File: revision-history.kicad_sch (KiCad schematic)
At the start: 0 parts

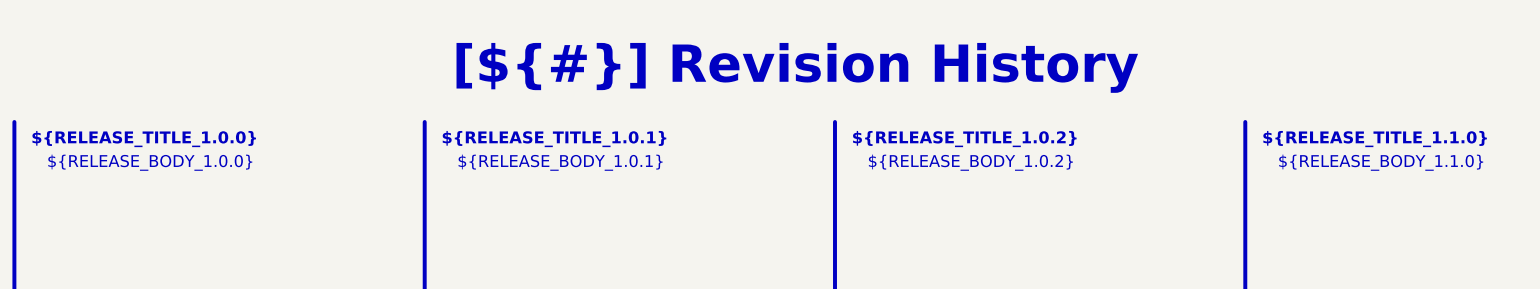
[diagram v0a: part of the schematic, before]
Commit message: feat: convert template to Boardwright
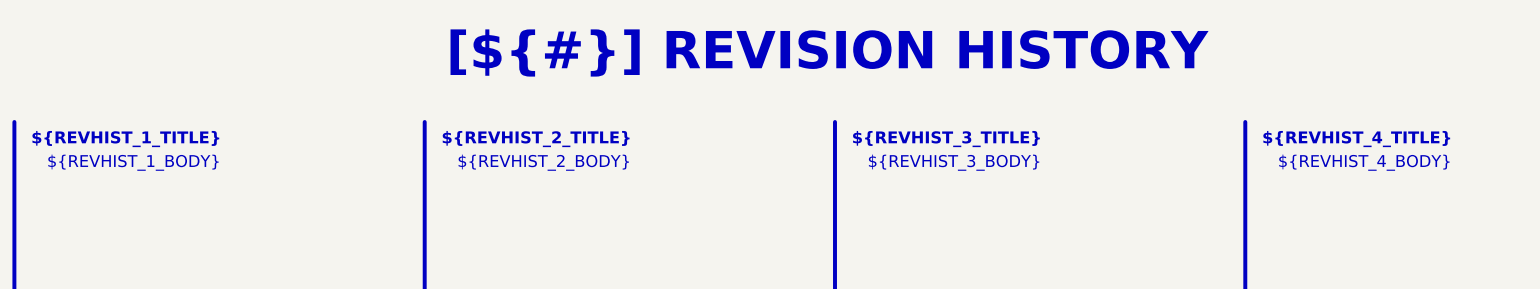
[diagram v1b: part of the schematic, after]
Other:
- title: Revision History -> REVISION HISTORY
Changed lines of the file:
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@@
 	(paper "A4")
 	(title_block
-		(title "Revision History")
+		(title "REVISION HISTORY")
 		(date "2025-01-12")
 		(rev "${REVISION}")
 		(company "${COMPANY}")
 	)
-	(text_box "${RELEASE_BODY_1.1.0}"
+	(text_box "${REVHIST_4_BODY}"
 		(exclude_from_sim no)
 		(at 224.79 35.56 0)
@@
 		(stroke
 			(width -0.0001)
-			(type default)
+			(type solid)
 		)
 		(fill
@@
 	(text_box "[${#}] ${TITLE}"
 		(exclude_from_sim no)
-		(at 80.01 15 0)
-		(size 137.16 15)
+		(at 20.32 10.16 0)
+		(size 266.7 20.32)
 		(margins 4.4999 4.4999 4.4999 4.4999)
 		(stroke
@@
 		)
 	)
-	(text_box "${RELEASE_BODY_1.0.0}"
+	(text_box "${REVHIST_1_BODY}"
 		(exclude_from_sim no)
 		(at 26.67 35.56 0)
@@
 		(stroke
 			(width -0.0001)
-			(type default)
+			(type solid)
 		)
 		(fill
@@
 		)
 	)
-	(text_box "${RELEASE_TITLE_1.0.2}"
+	(text_box "${REVHIST_3_TITLE}"
 		(exclude_from_sim no)
 		(at 156.21 31.75 0)
@@
 		(stroke
 			(width -0.0001)
-			(type default)
+			(type solid)
 		)
 		(fill
@@
 		)
 	)
-	(text_box "${RELEASE_BODY_1.0.2}"
+	(text_box "${REVHIST_3_BODY}"
 		(exclude_from_sim no)
 		(at 158.75 35.56 0)
@@
 		(stroke
 			(width -0.0001)
-			(type default)
+			(type solid)
 		)
 		(fill
@@
 		)
 	)
-	(text_box "${RELEASE_BODY_1.0.1}"
+	(text_box "${REVHIST_2_BODY}"
 		(exclude_from_sim no)
 		(at 92.71 35.56 0)
@@
 		(stroke
 			(width -0.0001)
-			(type default)
+			(type solid)
 		)
 		(fill
@@
 		)
 	)
-	(text_box "${RELEASE_TITLE_1.0.0}"
+	(text_box "${REVHIST_1_TITLE}"
 		(exclude_from_sim no)
 		(at 24.13 31.75 0)
@@
 		(stroke
 			(width -0.0001)
-			(type default)
+			(type solid)
 		)
 		(fill
@@
 		)
 	)
-	(text_box "${RELEASE_TITLE_1.0.1}"
+	(text_box "${REVHIST_2_TITLE}"
 		(exclude_from_sim no)
 		(at 90.17 31.75 0)
@@
 		(stroke
 			(width -0.0001)
-			(type default)
+			(type solid)
 		)
 		(fill
@@
 		)
 	)
-	(text_box "${RELEASE_TITLE_1.1.0}"
+	(text_box "${REVHIST_4_TITLE}"
 		(exclude_from_sim no)
 		(at 222.25 31.75 0)
@@
 		(stroke
 			(width -0.0001)
-			(type default)
+			(type solid)
 		)
 		(fill
